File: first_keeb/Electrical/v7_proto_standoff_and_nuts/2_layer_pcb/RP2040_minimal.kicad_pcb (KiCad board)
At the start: 2 copper layers, 77.4 x 77.1 mm, 71 parts, among them P1 USB-TYPE-C-016, Q1 SN74LV1T34DBV, SW1 SKRKAGE020, SW2 PTS647 SN70 SMTR2 LFS, SW3 PTS647 SN70 SMTR2 LFS, U1 NCP1117-3.3_SOT223, U2 LM4040DBZ-3, U3 PRTR5V0U2X, U4 W25Q32JVSS, U5 RP2040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

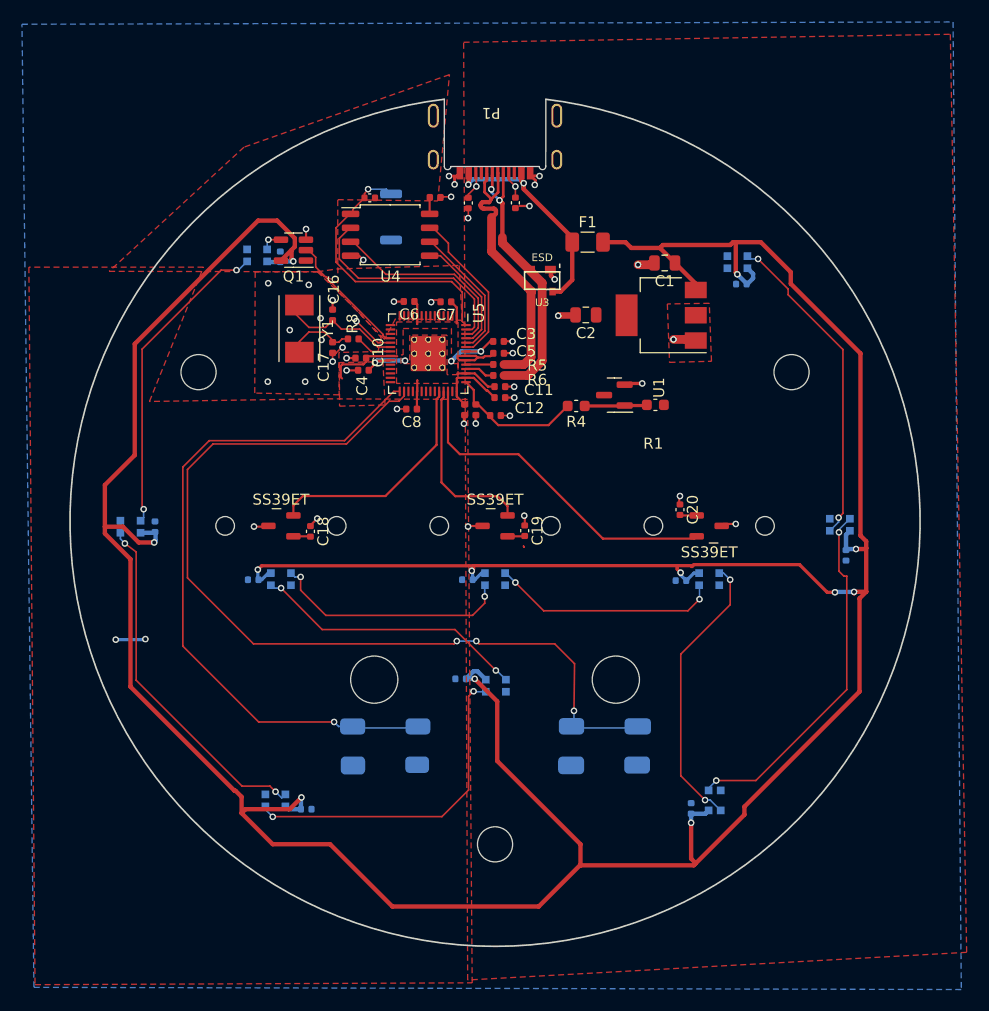
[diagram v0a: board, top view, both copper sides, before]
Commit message: adds 2 layer and 4 layer pcb versions
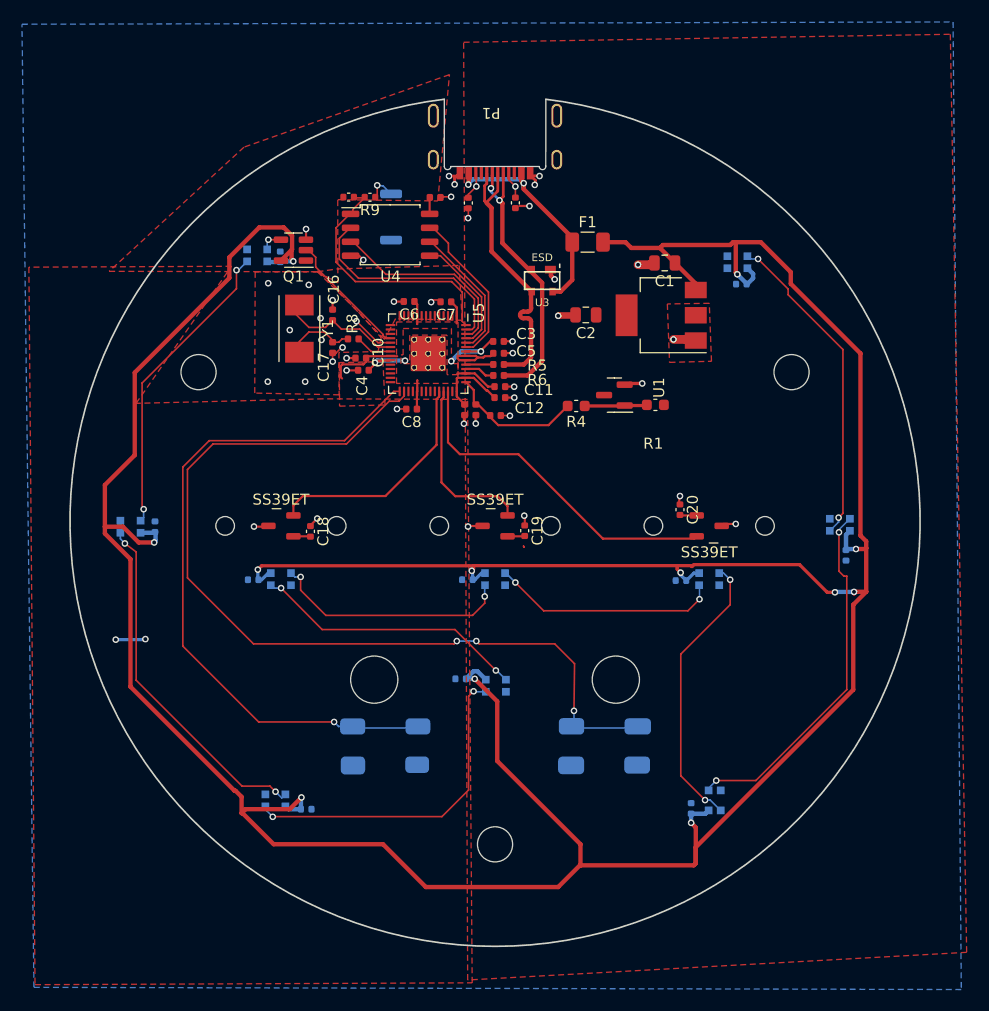
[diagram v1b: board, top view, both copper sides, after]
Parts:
- added R9: 1k, Capacitor_SMD:C_0402_1005Metric, F.Cu at (88.6, 70.1)
- SW1: value SKRKAGE020 -> SKRKAHE020
- moved R7 1.92 mm to (86.7, 70.1), turned to 0 degrees
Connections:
- SW1 pad 2: /QSPI_SS -> Net-(R9-Pad1)
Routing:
- net Net-(R9-Pad1): track 0.00 -> 2.79 mm, vias 0 -> 1
- net +5V: track 331.2 -> 328.6 mm
- net /QSPI_SS: track 25.9 -> 23.6 mm, vias 1 -> 0
- net Net-(D1-DOUT): track 28.7 -> 27.8 mm

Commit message: improve 3v3 traces in 2 layer board
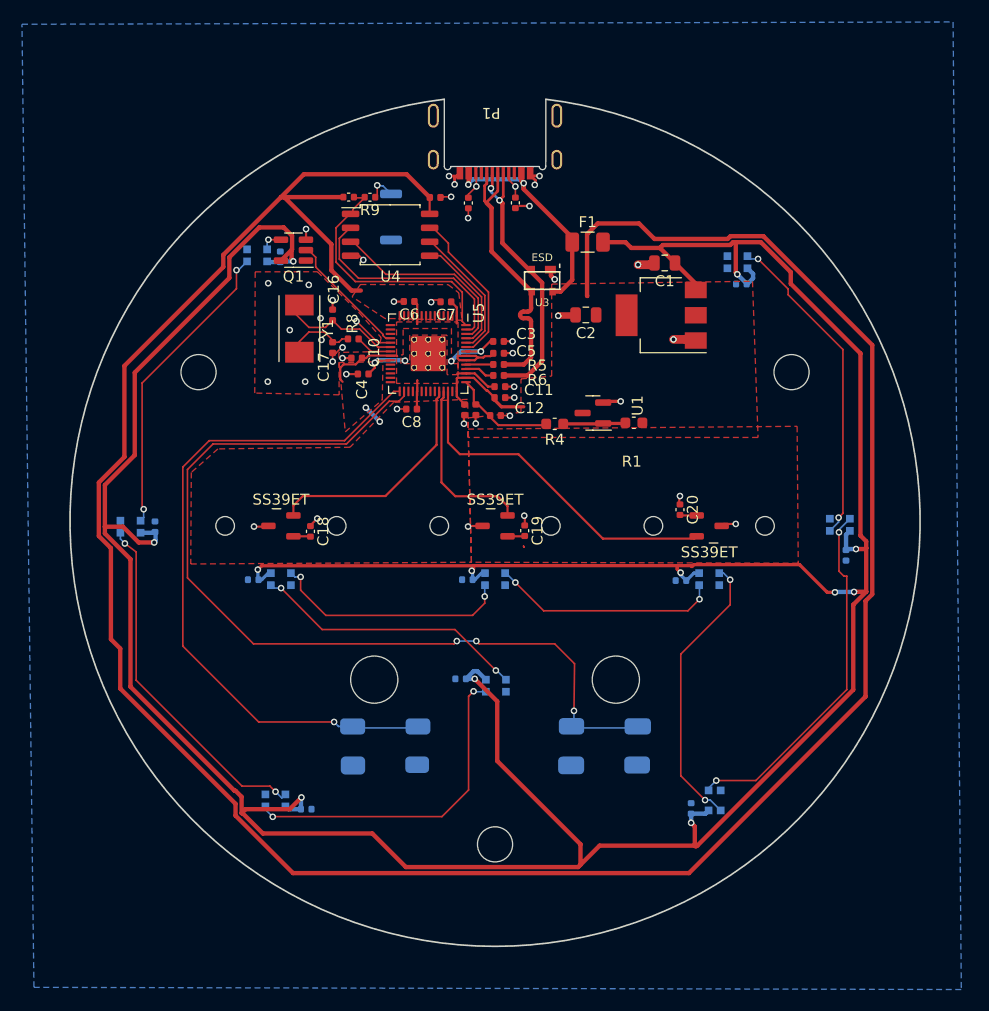
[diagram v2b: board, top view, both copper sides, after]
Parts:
- moved U2 2.55 mm to (108.9, 89.7)
- moved R1 2.55 mm to (112.6, 90.6)
- moved R4 2.55 mm to (105.4, 90.7)
- moved C10 0.37 mm to (87.4, 84.7)
- moved C4 0.34 mm to (88.0, 86.2)
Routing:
- net +3V3: track 36.5 -> 275.6 mm
- net +5V: track 328.6 -> 324.6 mm
- net ADC_AVDD: track 12.5 -> 9.77 mm

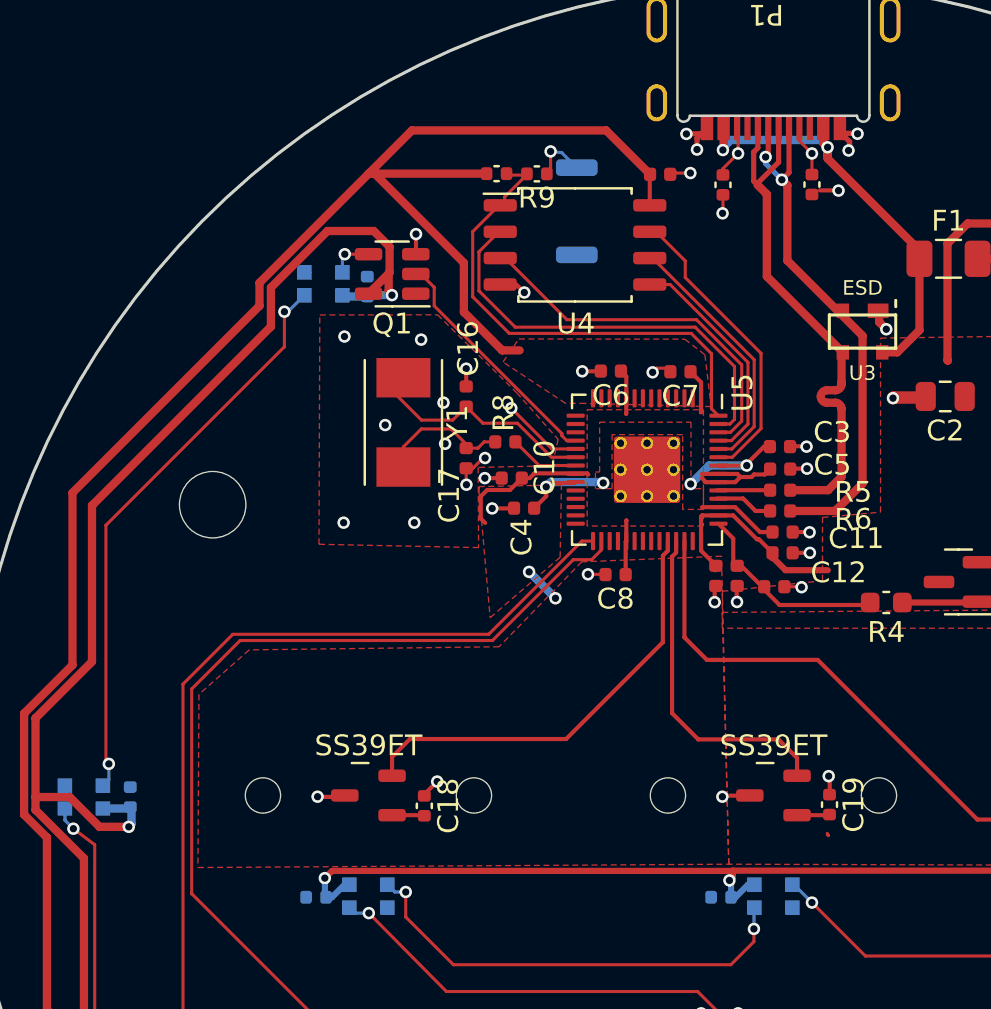
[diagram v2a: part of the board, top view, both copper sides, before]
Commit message: improve d+/d- traces
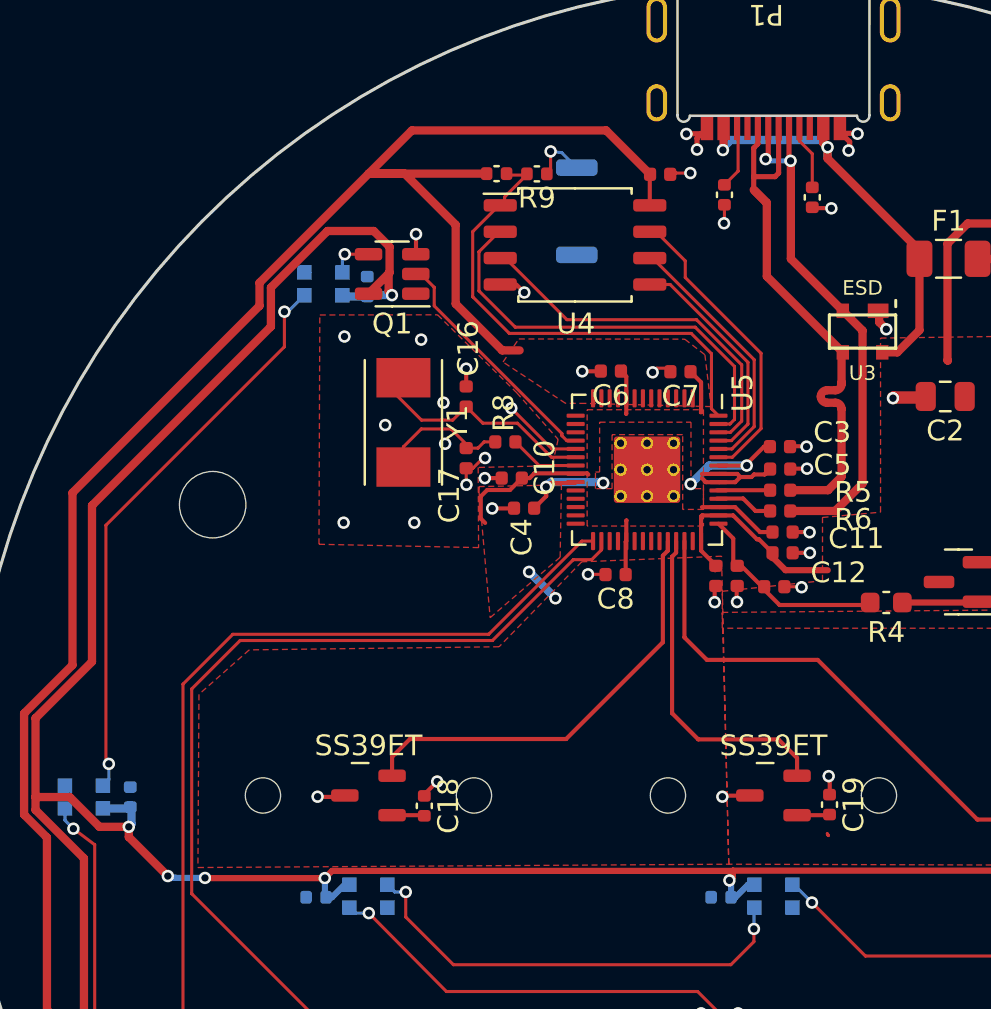
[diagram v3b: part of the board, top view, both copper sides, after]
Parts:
- moved R2 0.62 mm to (101.9, 71.2)
- moved R3 0.49 mm to (97.6, 71.1)
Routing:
- net +5V: track 324.6 -> 335.9 mm, vias 12 -> 14
- net /USB_D+: track 25.9 -> 26.9 mm
- net +3V3: track 275.6 -> 276.4 mm
- net Net-(P1-CC1): track 2.48 -> 3.10 mm, vias 1 -> 0
- net /USB_D-: track 25.7 -> 25.1 mm
- net Net-(P1-CC2): track 2.57 -> 3.02 mm, vias 1 -> 0
